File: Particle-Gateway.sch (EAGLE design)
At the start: 25 parts, among them J2 GROVE-I2C, J3 Lipo Battery, J4 GROVE-I2C, J5 CON_HEADER_1X08-PTH, P1 PADSMALL, U1 AMS1117-3.3

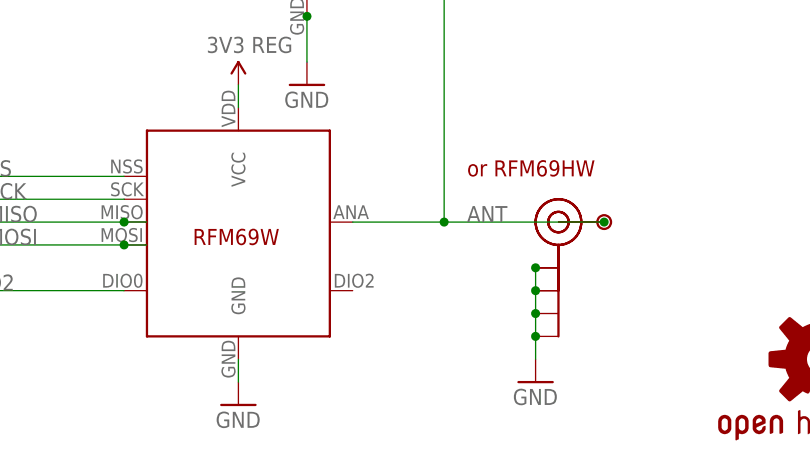
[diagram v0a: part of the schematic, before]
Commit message: Connect DIO2 to D3
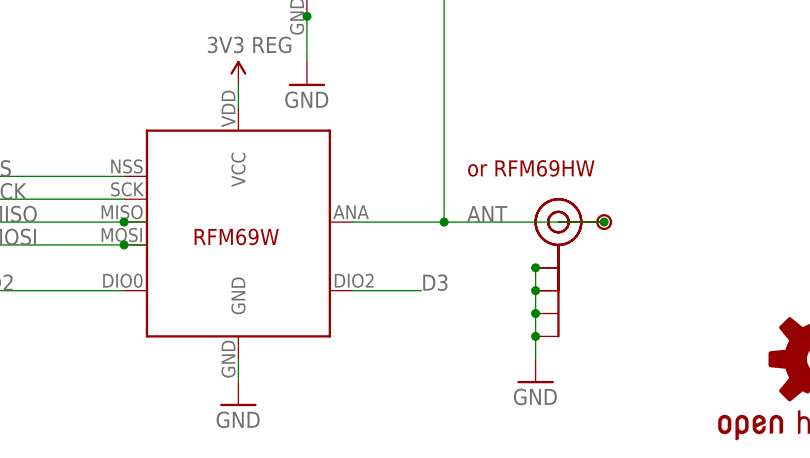
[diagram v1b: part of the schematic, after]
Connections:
- net D3: now also U$3.DIO2
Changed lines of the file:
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@@
 <?xml version="1.0" encoding="utf-8"?>
 <!DOCTYPE eagle SYSTEM "eagle.dtd">
-<eagle version="7.3.0">
+<eagle version="7.4.0">
 <drawing>
 <settings>
@@
 <pinref part="JP4" gate="G$1" pin="4"/>
 </segment>
-</net>
+<segment>
+<pinref part="U$3" gate="G$1" pin="DIO2"/>
+<wire x1="119.38" y1="22.86" x2="127" y2="22.86" width="0.1524" layer="91"/>
+<label x="127" y="22.86" size="1.778" layer="95"/>
+</segment>
+</net>
